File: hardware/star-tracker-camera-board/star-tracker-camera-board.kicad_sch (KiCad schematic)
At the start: 41 parts, among them J1 3-1734742-6, U1 AR0134CSSM00SPCA0, U2 TPS70618DRVR, U3 TPS71928-28DRVT, U4 TPS71928-28DRVT, X1 MC2520Z27.0000C19XSH

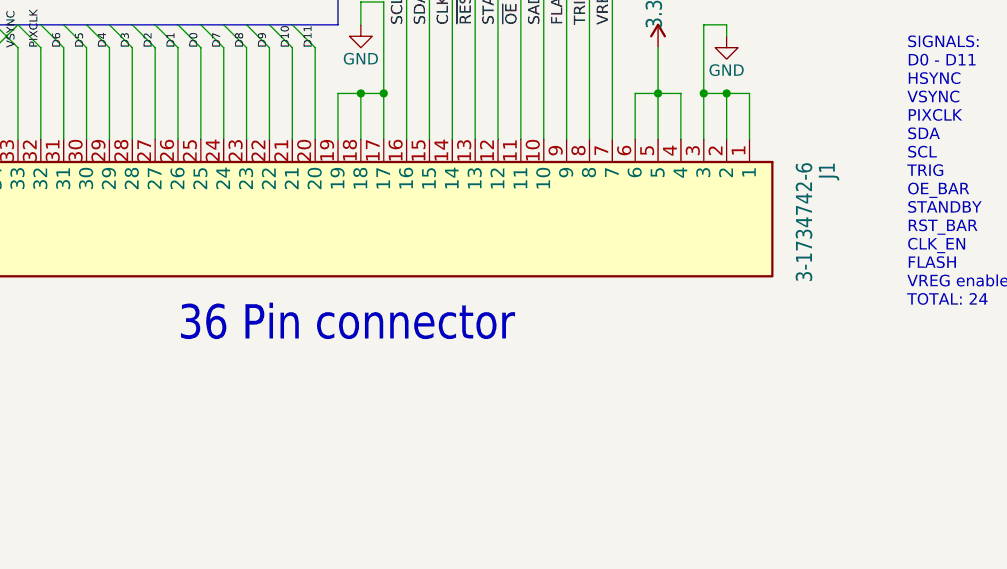
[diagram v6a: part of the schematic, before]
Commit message: Added FFC cable part number
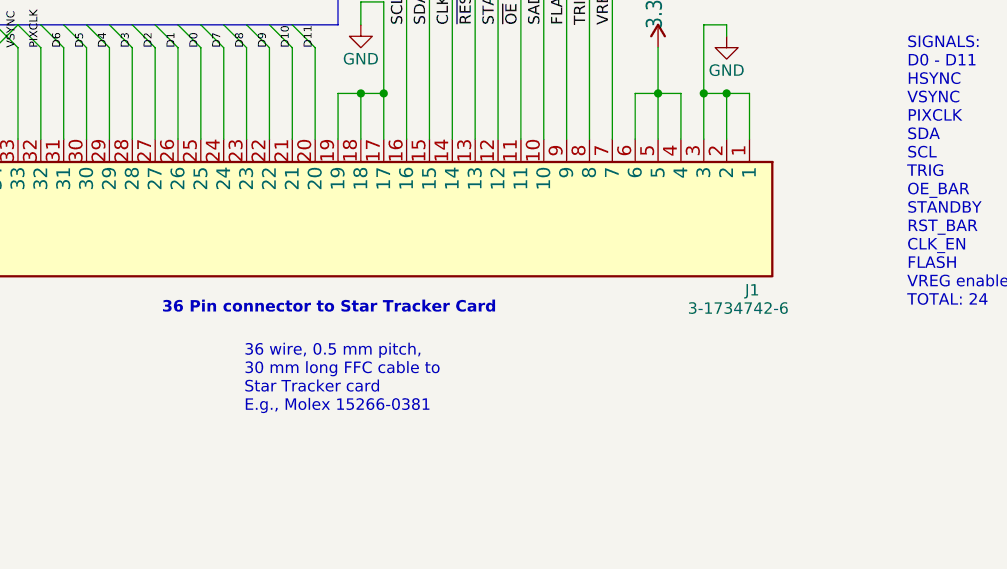
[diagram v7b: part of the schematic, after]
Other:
- note added: "36 Pin connector to Star Tracker Card"
- note added: "36 wire, 0.5 mm pitch, 30 mm long FFC cable to Star Tracker card E.g., Molex 15266-0381"
- note removed: "36 Pin connector"
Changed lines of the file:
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@@
 		)
 	)
-	(text "36 Pin connector"
+	(text "36 Pin connector to Star Tracker Card"
 		(exclude_from_sim no)
-		(at 88.9 218.44 0)
+		(at 87.122 215.138 0)
 		(effects
 			(font
-				(size 3.81 3.2385)
+				(size 1.27 1.27)
+				(thickness 0.254)
+				(bold yes)
 			)
 			(justify left bottom)
@@
 		)
 	)
+	(text "36 wire, 0.5 mm pitch, \n30 mm long FFC cable to\nStar Tracker card\nE.g., Molex 15266-0381"
+		(exclude_from_sim no)
+		(at 96.266 222.25 0)
+		(effects
+			(font
+				(size 1.27 1.27)
+			)
+			(justify left)
+		)
+	)
 	(text "VREG enable pulled high to enable. DNP pulldown resistor.\nPut VREG enable traces in a place I can cut them\nand enable then separately via test points"
 		(exclude_from_sim no)
@@
 		(dnp no)
 		(property "Reference" "J1"
-			(at 160.02 198.12 0)
+			(at 151.892 213.106 90)
 			(show_name no)
 			(do_not_autoplace no)
 			(effects
 				(font
-					(size 1.7808 1.5136)
+					(size 1.27 1.27)
 				)
 				(justify left bottom)
@@
 		)
 		(property "Value" "3-1734742-6"
-			(at 157.48 198.12 0)
+			(at 145.542 215.138 90)
 			(show_name no)
 			(do_not_autoplace no)
 			(effects
 				(font
-					(size 1.7799 1.5129)
+					(size 1.27 1.27)
 				)
 				(justify left bottom)
